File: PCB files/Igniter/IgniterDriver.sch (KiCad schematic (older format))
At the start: 10 parts

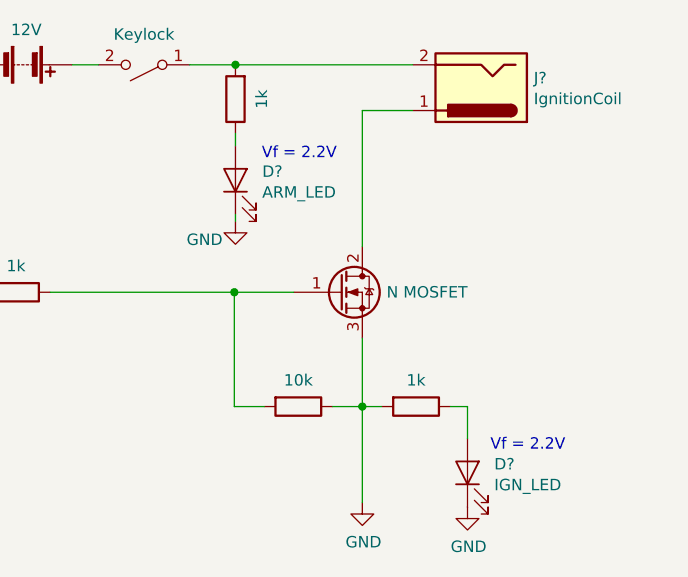
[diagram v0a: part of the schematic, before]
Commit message: 10/11
Arduino uno footprint
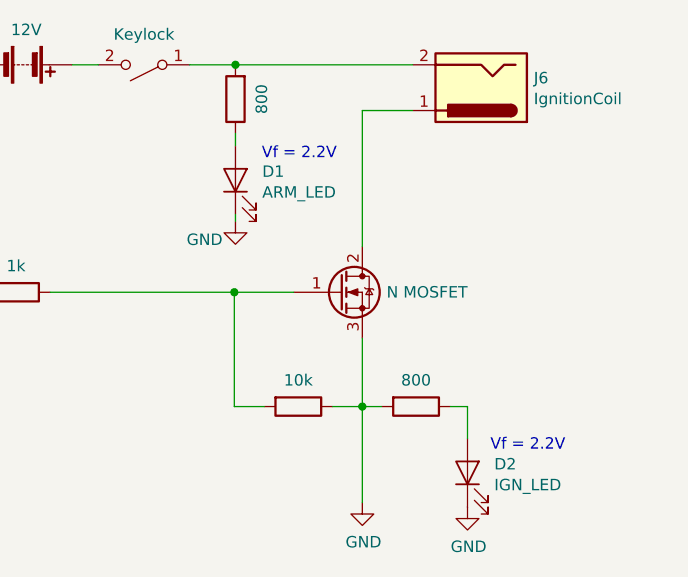
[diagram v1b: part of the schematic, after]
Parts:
- D1, D2: renamed from D?; footprint (none) -> LED_THT:LED_D3.0mm
- J6: renamed from J?; footprint (none) -> Connector_BarrelJack:BarrelJack_Horizontal
- R1, R3: renamed from R?; footprint (none) -> Resistor_THT:R_Axial_DIN0204_L3.6mm_D1.6mm_P5.08mm_Horizontal
- R2, R4: renamed from R?; value 1k -> 800; footprint (none) -> Resistor_THT:R_Axial_DIN0204_L3.6mm_D1.6mm_P5.08mm_Horizontal
- gave numbers to parts that had none: 3
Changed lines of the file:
@@
 $EndDescr
 $Comp
-L power:GND #PWR?
+L power:GND #PWR03
 U 1 1 5D9D4B7B
 P 5920 4925
-F 0 "#PWR?" H 5920 4675 50  0001 C CNN
+F 0 "#PWR03" H 5920 4675 50  0001 C CNN
 F 1 "GND" H 5925 4752 50  0000 C CNN
 F 2 "" H 5920 4925 50  0001 C CNN
@@
 $EndComp
 $Comp
-L Device:LED D?
+L Device:LED D2
 U 1 1 5D9D4B81
 P 6380 4795
-F 0 "D?" V 6418 4678 50  0000 R CNN
+F 0 "D2" V 6418 4678 50  0000 R CNN
 F 1 "IGN_LED" V 6327 4678 50  0000 R CNN
-F 2 "" H 6380 4795 50  0001 C CNN
+F 2 "LED_THT:LED_D3.0mm" H 6380 4795 50  0001 C CNN
 F 3 "~" H 6380 4795 50  0001 C CNN
 	1    6380 4795
@@
 	6380 4505 6380 4645
 $Comp
-L power:GND #PWR?
+L power:GND #PWR04
 U 1 1 5D9D4B88
 P 6380 4945
-F 0 "#PWR?" H 6380 4695 50  0001 C CNN
+F 0 "#PWR04" H 6380 4695 50  0001 C CNN
 F 1 "GND" H 6385 4772 50  0000 C CNN
 F 2 "" H 6380 4945 50  0001 C CNN
@@
 P 6440 3110
 AR Path="/5D9D4B91" Ref="J?"  Part="1"
-AR Path="/5D9BEB88/5D9D4B91" Ref="J?"  Part="1"
-F 0 "J?" H 6210 3068 50  0000 R CNN
+AR Path="/5D9BEB88/5D9D4B91" Ref="J6"  Part="1"
+F 0 "J6" H 6210 3068 50  0000 R CNN
 F 1 "IgnitionCoil" H 6210 3159 50  0000 R CNN
-F 2 "" H 6490 3070 50  0001 C CNN
+F 2 "Connector_BarrelJack:BarrelJack_Horizontal" H 6490 3070 50  0001 C CNN
 F 3 "~" H 6490 3070 50  0001 C CNN
 	1    6440 3110
@@
 	6005 4505 5920 4505
 $Comp
-L Device:R R?
+L Device:R R4
 U 1 1 5D9D4B9A
 P 6155 4505
-F 0 "R?" V 5948 4505 50  0001 C CNN
-F 1 "1k" V 6040 4505 50  0000 C CNN
-F 2 "" V 6085 4505 50  0001 C CNN
+F 0 "R4" V 5948 4505 50  0001 C CNN
+F 1 "800" V 6040 4505 50  0000 C CNN
+F 2 "Resistor_THT:R_Axial_DIN0204_L3.6mm_D1.6mm_P5.08mm_Horizontal" V 6085 4505 50  0001 C CNN
 F 3 "~" H 6155 4505 50  0001 C CNN
 	1    6155 4505
@@
 	5365 3695 5365 3665
 $Comp
-L power:GND #PWR?
+L power:GND #PWR02
 U 1 1 5D9D4BA1
 P 5365 3695
-F 0 "#PWR?" H 5365 3445 50  0001 C CNN
+F 0 "#PWR02" H 5365 3445 50  0001 C CNN
 F 1 "GND" H 5230 3615 50  0000 C CNN
 F 2 "" H 5365 3695 50  0001 C CNN
@@
 Connection ~ 5365 3010
 $Comp
-L Device:R R?
+L Device:R R2
 U 1 1 5D9D4BAA
 P 5365 3160
-F 0 "R?" V 5158 3160 50  0001 C CNN
-F 1 "1k" V 5250 3160 50  0000 C CNN
-F 2 "" V 5295 3160 50  0001 C CNN
+F 0 "R2" V 5158 3160 50  0001 C CNN
+F 1 "800" V 5250 3160 50  0000 C CNN
+F 2 "Resistor_THT:R_Axial_DIN0204_L3.6mm_D1.6mm_P5.08mm_Horizontal" V 5295 3160 50  0001 C CNN
 F 3 "~" H 5365 3160 50  0001 C CNN
 	1    5365 3160
@@
 	4250 3130 4250 3010
 $Comp
-L Device:Battery BT?
+L Device:Battery BT1
 U 1 1 5D9D4BB2
 P 4450 3010
-F 0 "BT?" V 4205 3010 50  0001 C CNN
+F 0 "BT1" V 4205 3010 50  0001 C CNN
 F 1 "12V" V 4297 3010 50  0000 C CNN
 F 2 "" V 4450 3070 50  0001 C CNN
@@
 	4650 3010 4765 3010
 $Comp
-L Device:LED D?
+L Device:LED D1
 U 1 1 5D9D4BB9
 P 5365 3515
-F 0 "D?" V 5403 3398 50  0000 R CNN
+F 0 "D1" V 5403 3398 50  0000 R CNN
 F 1 "ARM_LED" V 5312 3398 50  0000 R CNN
-F 2 "" H 5365 3515 50  0001 C CNN
+F 2 "LED_THT:LED_D3.0mm" H 5365 3515 50  0001 C CNN
 F 3 "~" H 5365 3515 50  0001 C CNN
 	1    5365 3515
@@
 $EndComp
 $Comp
-L power:GND #PWR?
+L power:GND #PWR01
 U 1 1 5D9D4BBF
 P 4250 3130
-F 0 "#PWR?" H 4250 2880 50  0001 C CNN
+F 0 "#PWR01" H 4250 2880 50  0001 C CNN
 F 1 "GND" H 4255 2957 50  0000 C CNN
 F 2 "" H 4250 3130 50  0001 C CNN
@@
 $EndComp
 $Comp
-L Switch:SW_SPST SW?
+L Switch:SW_SPST SW1
 U 1 1 5D9D4BC5
 P 4965 3010
-F 0 "SW?" H 4965 2785 50  0001 C CNN
+F 0 "SW1" H 4965 2785 50  0001 C CNN
 F 1 "Keylock" H 4965 2877 50  0000 C CNN
 F 2 "" H 4965 3010 50  0001 C CNN
@@
 	5920 4205 5920 4505
 $Comp
-L Device:Q_NMOS_GDS Q?
+L Device:Q_NMOS_GDS Q1
 U 1 1 5D9D4BD7
 P 5820 4005
-F 0 "Q?" H 6026 4051 50  0001 L CNN
+F 0 "Q1" H 6026 4051 50  0001 L CNN
 F 1 "N MOSFET" H 6026 4005 50  0000 L CNN
 F 2 "" H 6020 4105 50  0001 C CNN
@@
 $EndComp
 $Comp
-L Device:R R?
+L Device:R R3
 U 1 1 5D9D4BDD
 P 5640 4505
-F 0 "R?" V 5433 4505 50  0001 C CNN
+F 0 "R3" V 5433 4505 50  0001 C CNN
 F 1 "10k" V 5525 4505 50  0000 C CNN
-F 2 "" V 5570 4505 50  0001 C CNN
+F 2 "Resistor_THT:R_Axial_DIN0204_L3.6mm_D1.6mm_P5.08mm_Horizontal" V 5570 4505 50  0001 C CNN
 F 3 "~" H 5640 4505 50  0001 C CNN
 	1    5640 4505
@@
 $EndComp
 $Comp
-L Device:R R?
+L Device:R R1
 U 1 1 5D9D4BE3
 P 4405 4005
-F 0 "R?" V 4198 4005 50  0001 C CNN
+F 0 "R1" V 4198 4005 50  0001 C CNN
 F 1 "1k" V 4290 4005 50  0000 C CNN
-F 2 "" V 4335 4005 50  0001 C CNN
+F 2 "Resistor_THT:R_Axial_DIN0204_L3.6mm_D1.6mm_P5.08mm_Horizontal" V 4335 4005 50  0001 C CNN
 F 3 "~" H 4405 4005 50  0001 C CNN
 	1    4405 4005

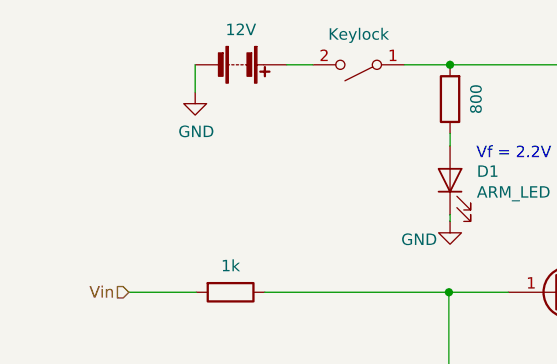
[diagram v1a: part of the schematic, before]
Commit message: 10/15/2019
-Minor schematic edits
-Rearranged some symbols
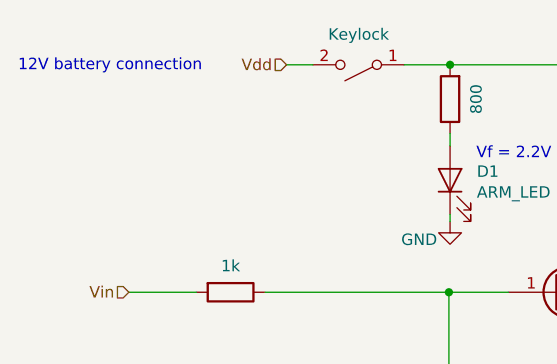
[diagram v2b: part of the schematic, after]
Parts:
- removed BT1: 12V, symbol Device:Battery
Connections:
- net Vdd: now reaches SW1.2 (B)
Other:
- note added: "12V battery connection"
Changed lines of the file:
@@
 LIBS:interface
 LIBS:Igniter-cache
-EELAYER 29 0
+EELAYER 26 0
 EELAYER END
 $Descr A4 11693 8268
@@
 	5165 3010 5365 3010
 Wire Wire Line
-	4250 3130 4250 3010
-$Comp
-L Device:Battery BT1
-U 1 1 5D9D4BB2
-P 4450 3010
-F 0 "BT1" V 4205 3010 50  0001 C CNN
-F 1 "12V" V 4297 3010 50  0000 C CNN
-F 2 "" V 4450 3070 50  0001 C CNN
-F 3 "~" V 4450 3070 50  0001 C CNN
-	1    4450 3010
-	0    1    1    0
-$EndComp
-Wire Wire Line
 	4650 3010 4765 3010
 $Comp
@@
 $EndComp
 $Comp
-L power:GND #PWR01
-U 1 1 5D9D4BBF
-P 4250 3130
-F 0 "#PWR01" H 4250 2880 50  0001 C CNN
-F 1 "GND" H 4255 2957 50  0000 C CNN
-F 2 "" H 4250 3130 50  0001 C CNN
-F 3 "" H 4250 3130 50  0001 C CNN
-	1    4250 3130
-	1    0    0    -1
-$EndComp
-$Comp
 L Switch:SW_SPST SW1
 U 1 1 5D9D4BC5
@@
 Wire Wire Line
 	4555 4005 5360 4005
+Text HLabel 4650 3010 0    50   Input ~ 0
+Vdd
+Text Notes 3475 3045 0    50   ~ 0
+12V battery connection
 $EndSCHEMATC

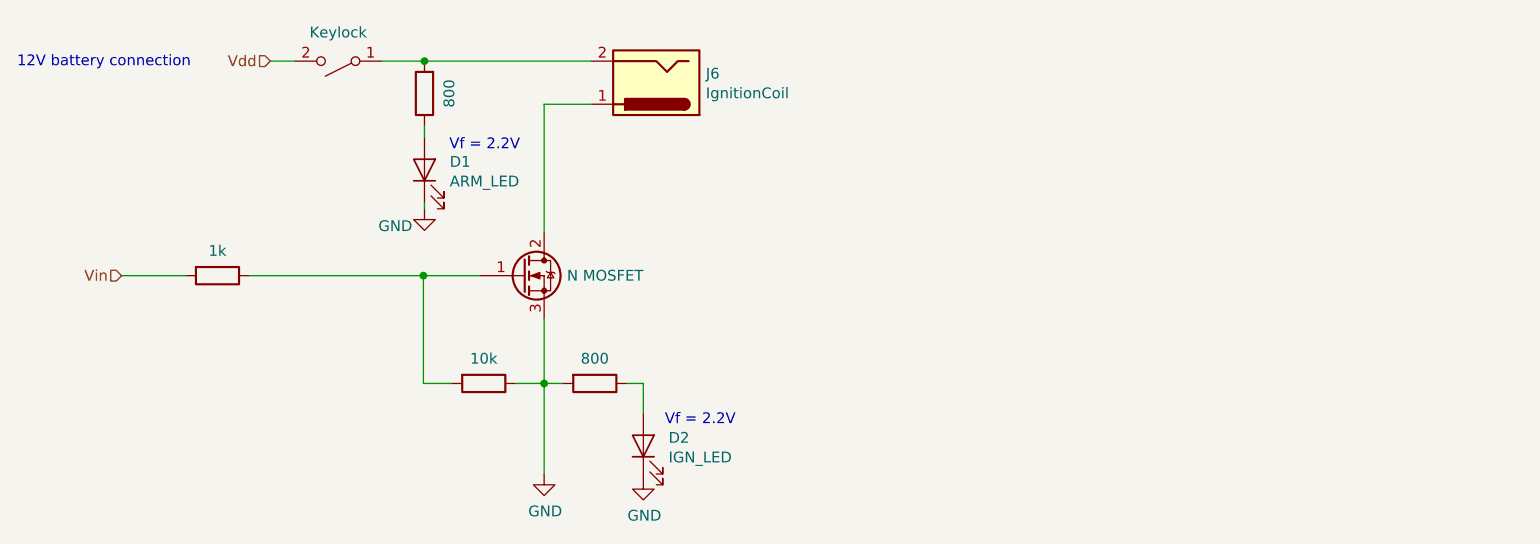
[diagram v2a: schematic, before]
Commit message: 10/19/2019
BIG updates
-Reorganized entire schematic
-Every functional block has a label now
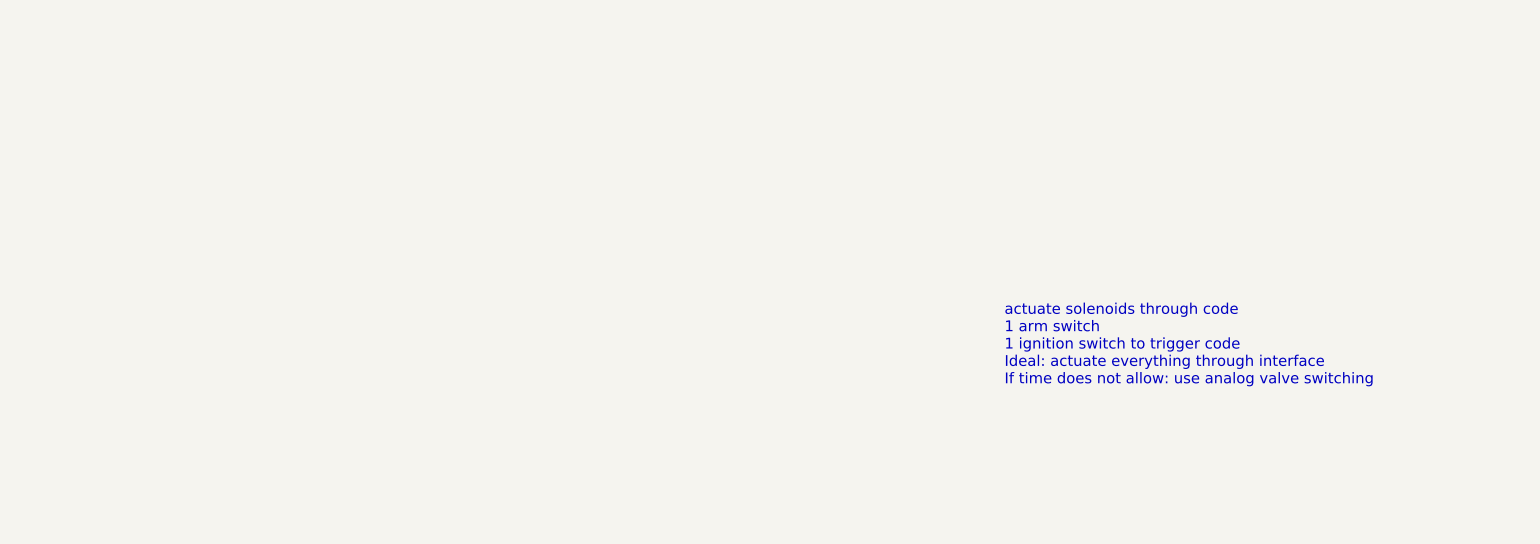
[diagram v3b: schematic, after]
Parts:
- removed D1: ARM_LED, LED_THT:LED_D3.0mm, symbol Device:LED
- removed D2: IGN_LED, LED_THT:LED_D3.0mm, symbol Device:LED
- removed J6: IgnitionCoil, Connector_BarrelJack:BarrelJack_Horizontal, symbol Connector:Barrel_Jack
- removed Q1: N MOSFET, symbol Device:Q_NMOS_GDS
- removed R1: 1k, Resistor_THT:R_Axial_DIN0204_L3.6mm_D1.6mm_P5.08mm_Horizontal, symbol Device:R
- removed R2, R4: 800, Resistor_THT:R_Axial_DIN0204_L3.6mm_D1.6mm_P5.08mm_Horizontal, symbol Device:R
- removed R3: 10k, Resistor_THT:R_Axial_DIN0204_L3.6mm_D1.6mm_P5.08mm_Horizontal, symbol Device:R
- removed SW1: Keylock, symbol Switch:SW_SPST
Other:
- note added: "actuate solenoids through code\n1 arm switch\n1 ignition switch to trigger code\nIdeal: actuate everything through interface\nIf time does not allow: use analog valve switching\n"
- note removed: "12V battery connection"
- note removed: "Vf = 2.2V\n"
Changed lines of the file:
@@
 Comment4 ""
 $EndDescr
-$Comp
-L power:GND #PWR03
-U 1 1 5D9D4B7B
-P 5920 4925
-F 0 "#PWR03" H 5920 4675 50  0001 C CNN
-F 1 "GND" H 5925 4752 50  0000 C CNN
-F 2 "" H 5920 4925 50  0001 C CNN
-F 3 "" H 5920 4925 50  0001 C CNN
-	1    5920 4925
-	1    0    0    -1
-$EndComp
-$Comp
-L Device:LED D2
-U 1 1 5D9D4B81
-P 6380 4795
-F 0 "D2" V 6418 4678 50  0000 R CNN
-F 1 "IGN_LED" V 6327 4678 50  0000 R CNN
-F 2 "LED_THT:LED_D3.0mm" H 6380 4795 50  0001 C CNN
-F 3 "~" H 6380 4795 50  0001 C CNN
-	1    6380 4795
-	0    -1   -1   0
-$EndComp
-Wire Wire Line
-	6380 4505 6380 4645
-$Comp
-L power:GND #PWR04
-U 1 1 5D9D4B88
-P 6380 4945
-F 0 "#PWR04" H 6380 4695 50  0001 C CNN
-F 1 "GND" H 6385 4772 50  0000 C CNN
-F 2 "" H 6380 4945 50  0001 C CNN
-F 3 "" H 6380 4945 50  0001 C CNN
-	1    6380 4945
-	1    0    0    -1
-$EndComp
-Text Notes 6480 4705 0    50   ~ 0
-Vf = 2.2V\n
-Wire Wire Line
-	5920 3210 6140 3210
-Wire Wire Line
-	5365 3010 6140 3010
-$Comp
-L Connector:Barrel_Jack J?
-U 1 1 5D9D4B91
-P 6440 3110
-AR Path="/5D9D4B91" Ref="J?"  Part="1"
-AR Path="/5D9BEB88/5D9D4B91" Ref="J6"  Part="1"
-F 0 "J6" H 6210 3068 50  0000 R CNN
-F 1 "IgnitionCoil" H 6210 3159 50  0000 R CNN
-F 2 "Connector_BarrelJack:BarrelJack_Horizontal" H 6490 3070 50  0001 C CNN
-F 3 "~" H 6490 3070 50  0001 C CNN
-	1    6440 3110
-	-1   0    0    1
-$EndComp
-Text Notes 5480 3430 0    50   ~ 0
-Vf = 2.2V\n
-Wire Wire Line
-	6305 4505 6380 4505
-Wire Wire Line
-	6005 4505 5920 4505
-$Comp
-L Device:R R4
-U 1 1 5D9D4B9A
-P 6155 4505
-F 0 "R4" V 5948 4505 50  0001 C CNN
-F 1 "800" V 6040 4505 50  0000 C CNN
-F 2 "Resistor_THT:R_Axial_DIN0204_L3.6mm_D1.6mm_P5.08mm_Horizontal" V 6085 4505 50  0001 C CNN
-F 3 "~" H 6155 4505 50  0001 C CNN
-	1    6155 4505
-	0    1    1    0
-$EndComp
-Wire Wire Line
-	5365 3695 5365 3665
-$Comp
-L power:GND #PWR02
-U 1 1 5D9D4BA1
-P 5365 3695
-F 0 "#PWR02" H 5365 3445 50  0001 C CNN
-F 1 "GND" H 5230 3615 50  0000 C CNN
-F 2 "" H 5365 3695 50  0001 C CNN
-F 3 "" H 5365 3695 50  0001 C CNN
-	1    5365 3695
-	1    0    0    -1
-$EndComp
-Wire Wire Line
-	5920 3210 5920 3805
-Wire Wire Line
-	5365 3365 5365 3310
-Connection ~ 5365 3010
-$Comp
-L Device:R R2
-U 1 1 5D9D4BAA
-P 5365 3160
-F 0 "R2" V 5158 3160 50  0001 C CNN
-F 1 "800" V 5250 3160 50  0000 C CNN
-F 2 "Resistor_THT:R_Axial_DIN0204_L3.6mm_D1.6mm_P5.08mm_Horizontal" V 5295 3160 50  0001 C CNN
-F 3 "~" H 5365 3160 50  0001 C CNN
-	1    5365 3160
-	-1   0    0    1
-$EndComp
-Wire Wire Line
-	5165 3010 5365 3010
-Wire Wire Line
-	4650 3010 4765 3010
-$Comp
-L Device:LED D1
-U 1 1 5D9D4BB9
-P 5365 3515
-F 0 "D1" V 5403 3398 50  0000 R CNN
-F 1 "ARM_LED" V 5312 3398 50  0000 R CNN
-F 2 "LED_THT:LED_D3.0mm" H 5365 3515 50  0001 C CNN
-F 3 "~" H 5365 3515 50  0001 C CNN
-	1    5365 3515
-	0    -1   -1   0
-$EndComp
-$Comp
-L Switch:SW_SPST SW1
-U 1 1 5D9D4BC5
-P 4965 3010
-F 0 "SW1" H 4965 2785 50  0001 C CNN
-F 1 "Keylock" H 4965 2877 50  0000 C CNN
-F 2 "" H 4965 3010 50  0001 C CNN
-F 3 "~" H 4965 3010 50  0001 C CNN
-	1    4965 3010
-	-1   0    0    1
-$EndComp
-Connection ~ 5920 4505
-Wire Wire Line
-	5920 4505 5920 4925
-Wire Wire Line
-	5360 4005 5620 4005
-Connection ~ 5360 4005
-Wire Wire Line
-	5360 4505 5360 4005
-Wire Wire Line
-	5490 4505 5360 4505
-Wire Wire Line
-	4255 4005 3960 4005
-Wire Wire Line
-	5920 4505 5790 4505
-Wire Wire Line
-	5920 4205 5920 4505
-$Comp
-L Device:Q_NMOS_GDS Q1
-U 1 1 5D9D4BD7
-P 5820 4005
-F 0 "Q1" H 6026 4051 50  0001 L CNN
-F 1 "N MOSFET" H 6026 4005 50  0000 L CNN
-F 2 "" H 6020 4105 50  0001 C CNN
-F 3 "~" H 5820 4005 50  0001 C CNN
-	1    5820 4005
-	1    0    0    -1
-$EndComp
-$Comp
-L Device:R R3
-U 1 1 5D9D4BDD
-P 5640 4505
-F 0 "R3" V 5433 4505 50  0001 C CNN
-F 1 "10k" V 5525 4505 50  0000 C CNN
-F 2 "Resistor_THT:R_Axial_DIN0204_L3.6mm_D1.6mm_P5.08mm_Horizontal" V 5570 4505 50  0001 C CNN
-F 3 "~" H 5640 4505 50  0001 C CNN
-	1    5640 4505
-	0    1    1    0
-$EndComp
-$Comp
-L Device:R R1
-U 1 1 5D9D4BE3
-P 4405 4005
-F 0 "R1" V 4198 4005 50  0001 C CNN
-F 1 "1k" V 4290 4005 50  0000 C CNN
-F 2 "Resistor_THT:R_Axial_DIN0204_L3.6mm_D1.6mm_P5.08mm_Horizontal" V 4335 4005 50  0001 C CNN
-F 3 "~" H 4405 4005 50  0001 C CNN
-	1    4405 4005
-	0    1    1    0
-$EndComp
-Text HLabel 3960 4005 0    50   Input ~ 0
-Vin
-Wire Wire Line
-	4555 4005 5360 4005
-Text HLabel 4650 3010 0    50   Input ~ 0
-Vdd
-Text Notes 3475 3045 0    50   ~ 0
-12V battery connection
+Text Notes 8055 4520 0    50   ~ 0
+actuate solenoids through code\n1 arm switch\n1 ignition switch to trigger code\nIdeal: actuate everything through interface\nIf time does not allow: use analog valve switching\n
 $EndSCHEMATC
